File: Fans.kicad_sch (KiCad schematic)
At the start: 8 parts, among them J7 Conn_01x06, Q1 PSMN8R5-40MSDX, Q2 PSMN8R5-40MSDX

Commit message: schematic
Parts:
- removed Q1, Q2: PSMN8R5-40MSDX, BUK7M1780EX, symbol utsvt_power:PSMN8R5-40MSDX
- added D5, D7: 1N4148WT, Diode_SMD:D_SOD-523, symbol Diode:1N4148WT
- added D6, D9: LED, symbol Device:LED
- added LVPWR3, LVPWR4, LVPWR5, LVPWR6: LED, LED_SMD:LED_0603_1608Metric, symbol Device:LED
- added Q1, Q5: PSMN8R5-40MSDX, BUK7M1780EX, symbol Simulation_SPICE:NMOS
- added R15, R4, R5, R8: 260, symbol Device:R
- added R19, R20: 4.3k, symbol Device:R
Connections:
- net FANS_POS: now also D5.1 (K), D7.1 (K)
- net FAN_A_NEG: now also D6.1 (K), D7.2 (A), Q5.1 (D)
- net FAN_A_TACHO: now also R5.2
- net FAN_B_NEG: now also D5.2 (A), D9.1 (K), Q1.1 (D)
- net FAN_B_TACHO: now also R8.2
- net GND: now also LVPWR3.1 (K), LVPWR4.1 (K), LVPWR5.1 (K), LVPWR6.1 (K), Q1.3 (S), Q5.3 (S)
- net PWM_FAN_A: now also R4.2
- net PWM_FAN_B: now also R15.2
- net at R_G2.1, R_PD2.2: now also Q1.2 (G)
- net at R_G1.1, R_PD1.2: now also Q5.2 (G)
- new net: LVPWR5.2 (A), R8.1
- new net: D9.2 (A), R20.1
- new net: LVPWR6.2 (A), R15.1
- new net: LVPWR4.2 (A), R5.1
- new net: LVPWR3.2 (A), R4.1
- new net: D6.2 (A), R19.1
- new net +24V: R19.2, R20.2
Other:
- note added: "Flyback Diodes"
- note added: "Indicator LEDs"
- note added: "put close to fan connector and mosfet for small inductive loop"
- moved on the sheet: J7, R10, R_G1, R_PD1, R_PD2

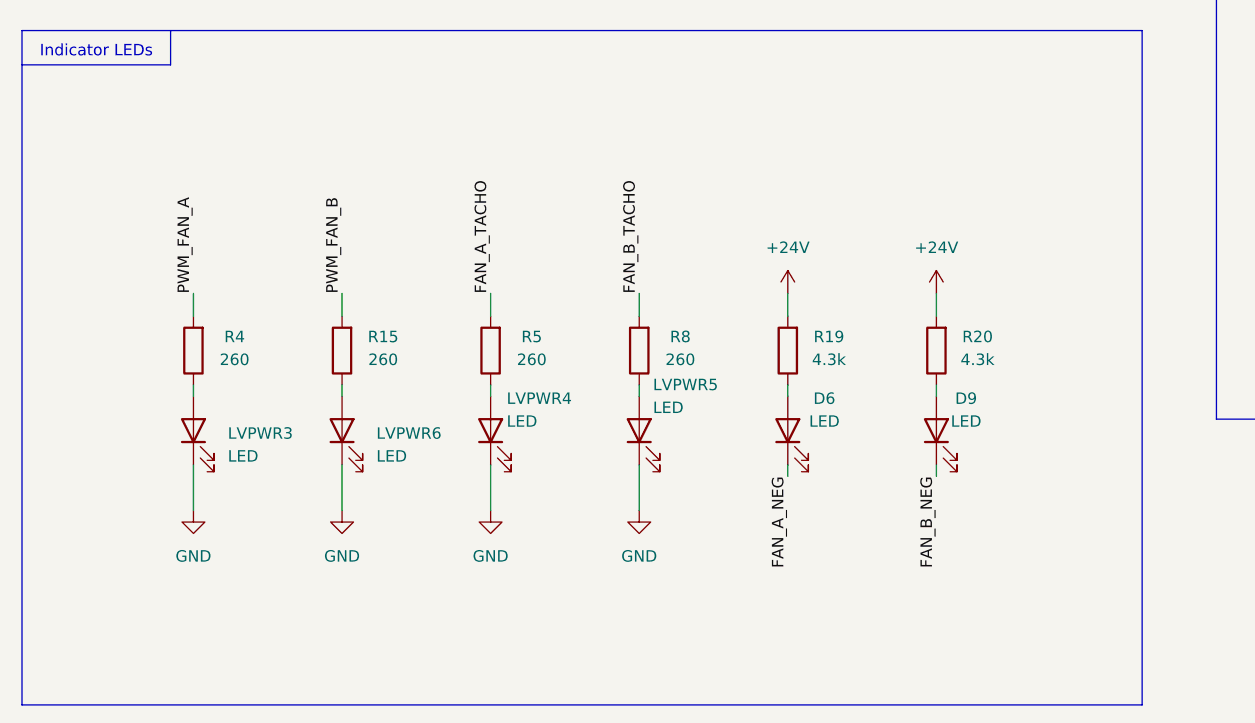
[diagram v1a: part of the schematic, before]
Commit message: added testpoints too
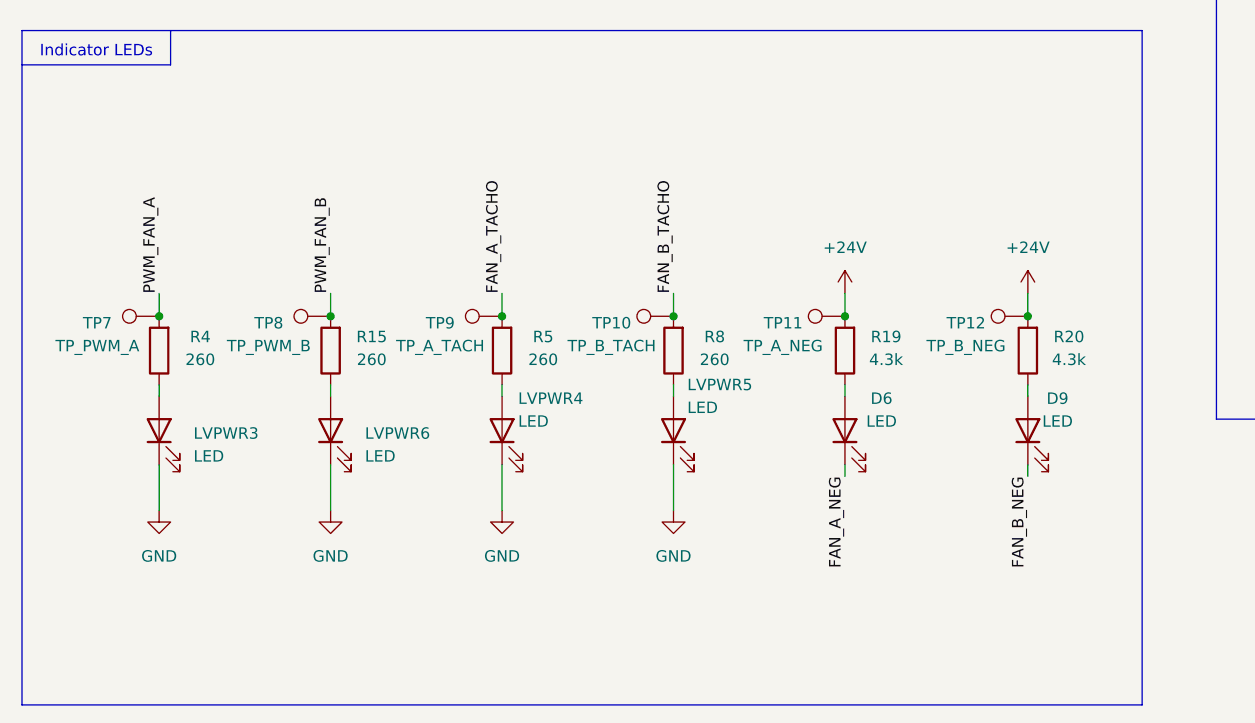
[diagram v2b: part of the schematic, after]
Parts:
- added TP10: TP_B_TACH, symbol Connector:TestPoint
- added TP11: TP_A_NEG, symbol Connector:TestPoint
- added TP12: TP_B_NEG, symbol Connector:TestPoint
- added TP7: TP_PWM_A, symbol Connector:TestPoint
- added TP8: TP_PWM_B, symbol Connector:TestPoint
- added TP9: TP_A_TACH, symbol Connector:TestPoint
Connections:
- net +24V: now also TP11.1, TP12.1
- net FAN_A_TACHO: now also TP9.1
- net FAN_B_TACHO: now also TP10.1
- net PWM_FAN_A: now also TP7.1
- net PWM_FAN_B: now also TP8.1
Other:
- moved on the sheet: D6, D9, LVPWR3, LVPWR4, LVPWR5, LVPWR6, R15, R19, R20, R4, R5, R8

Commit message: changes + ioc
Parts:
- removed LVPWR4, LVPWR5: LED, LED_SMD:LED_0603_1608Metric, symbol Device:LED
- removed R5, R8: 260, symbol Device:R
- removed TP10: TP_B_TACH, symbol Connector:TestPoint
- removed TP9: TP_A_TACH, symbol Connector:TestPoint
- R15, R4: value 260 -> 5k
- R19, R20: value 4.3k -> 5k
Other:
- moved on the sheet: D6, D9, LVPWR3, LVPWR6, R15, R19, R20, R4, TP11, TP12, TP7, TP8

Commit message: layout
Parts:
- removed D6, D9: LED, symbol Device:LED
- removed Q1, Q5: PSMN8R5-40MSDX, BUK7M1780EX, symbol Simulation_SPICE:NMOS
- added LVPWR16, LVPWR17: LED, LED_SMD:LED_0603_1608Metric, symbol Device:LED
- added Q1, Q5: PSMN8R5-40MSDX, UTSVT_Power:PSMN8R5-40MSDX, symbol UTSVT_Power:PSMN8R5-40MSDX
- D5, D7: Manufacturer_Part_Number (none) -> NCD0603R1
- J7: footprint (none) -> Connector_Molex:Molex_Nano-Fit_105310-xx06_2x03_P2.50mm_Vertical
- R10: footprint (none) -> Resistor_SMD:R_0603_1608Metric_Pad0.98x0.95mm_HandSolder; Manufacturer_Part_Number (none) -> CRCW06030000Z0EE
- R15, R19, R20, R4: value 5k -> 4.3k; footprint (none) -> Resistor_SMD:R_0603_1608Metric_Pad0.98x0.95mm_HandSolder; Manufacturer_Part_Number (none) -> CRCW06034K30FKEA
- R_G1, R_G2: footprint (none) -> Resistor_SMD:R_0603_1608Metric_Pad0.98x0.95mm_HandSolder; Manufacturer_Part_Number (none) -> CRCW0603120RFKEC
- R_PD1, R_PD2: footprint (none) -> Resistor_SMD:R_0603_1608Metric_Pad0.98x0.95mm_HandSolder; Manufacturer_Part_Number (none) -> CRCW060310K0FKEI
- TP11, TP12, TP7, TP8: footprint (none) -> TestPoint:TestPoint_Pad_1.0x1.0mm
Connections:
- net FAN_A_NEG: now also LVPWR16.1 (K), Q1.10 (D_6), Q1.11 (D_7), Q1.5 (D_1), Q1.6 (D_2), Q1.7 (D_3), Q1.8 (D_4), Q1.9 (D_5)
- net FAN_B_NEG: now also LVPWR17.1 (K), Q5.10 (D_6), Q5.11 (D_7), Q5.5 (D_1), Q5.6 (D_2), Q5.7 (D_3), Q5.8 (D_4), Q5.9 (D_5)
- net GND: now also Q1.1 (S_1), Q1.2 (S_2), Q1.3 (S_3), Q5.1 (S_1), Q5.2 (S_2), Q5.3 (S_3)
- net at R_G2.1, R_PD2.2: now also Q5.4 (G)
- net at R20.1: now also LVPWR17.2 (A)
- net at R_G1.1, R_PD1.2: now also Q1.4 (G)
- net at R19.1: now also LVPWR16.2 (A)
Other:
- moved on the sheet: R_G1, R_PD1

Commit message: added more
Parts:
- J7: footprint Connector_Molex:Molex_Nano-Fit_105310-xx06_2x03_P2.50mm_Vertical -> Connector_Molex:Molex_Nano-Fit_105309-xx06_1x06_P2.50mm_Vertical
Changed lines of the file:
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@@
 			)
 		)
-		(property "Footprint" "Connector_Molex:Molex_Nano-Fit_105310-xx06_2x03_P2.50mm_Vertical"
+		(property "Footprint" "Connector_Molex:Molex_Nano-Fit_105309-xx06_1x06_P2.50mm_Vertical"
 			(at 201.93 44.45 0)
 			(effects

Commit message: fon
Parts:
- renumbered TP7 to PWM_A2, TP8 to PWM_B2
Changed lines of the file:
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@@
 		(on_board yes)
 		(dnp no)
-		(property "Reference" "TP7"
+		(property "Reference" "PWM_A2"
 			(at 38.862 146.812 90)
 			(effects
@@
 			(project ""
 				(path "/a2e13c19-ff3a-4e43-a7f5-200fd5b2b978/26b9ca43-4422-48e7-9562-1bb32842f27e"
-					(reference "TP7")
+					(reference "PWM_A2")
 					(unit 1)
 				)
@@
 		(on_board yes)
 		(dnp no)
-		(property "Reference" "TP8"
+		(property "Reference" "PWM_B2"
 			(at 57.912 146.812 90)
 			(effects
@@
 			(project "PS-MotorControllerInterfacePCB"
 				(path "/a2e13c19-ff3a-4e43-a7f5-200fd5b2b978/26b9ca43-4422-48e7-9562-1bb32842f27e"
-					(reference "TP8")
-					(unit 1)
-				)
+					(reference "PWM_B2")
+					(unit 1)
+				)

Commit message: hello
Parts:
- removed TP11: TP_A_NEG, TestPoint:TestPoint_Pad_1.0x1.0mm, symbol Connector:TestPoint
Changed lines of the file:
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@@
 	)
 	(junction
-		(at 86.36 146.05)
-		(diameter 0)
-		(color 0 0 0 0)
-	)
-	(junction
 		(at 64.77 146.05)
 		(diameter 0)
@@
 					(unit 1)
 				)
-			)
-		)
-	)
-	(symbol
-		(lib_id "Connector:TestPoint")
-		(at 86.36 146.05 90)
-		(unit 1)
-		(exclude_from_sim no)
-		(in_bom yes)
-		(on_board yes)
-		(dnp no)
-		(property "Reference" "TP11"
-			(at 79.502 146.812 90)
-			(effects
-				(font
-					(size 1.27 1.27)
-				)
-			)
-		)
-		(property "Value" "TP_A_NEG"
-			(at 79.502 149.352 90)
-			(effects
-				(font
-					(size 1.27 1.27)
-				)
-			)
-		)
-		(property "Footprint" "TestPoint:TestPoint_Pad_1.0x1.0mm"
-			(at 86.36 140.97 0)
-			(effects
-				(font
-					(size 1.27 1.27)
-				)
-				(hide yes)
-			)
-		)
-		(property "Datasheet" "~"
-			(at 86.36 140.97 0)
-			(effects
-				(font
-					(size 1.27 1.27)
-				)
-				(hide yes)
-			)
-		)
-		(property "Description" "test point"
-			(at 86.36 146.05 0)
-			(effects
-				(font
-					(size 1.27 1.27)
-				)
-				(hide yes)
-			)
-		)
-		(property "Manufacturer" ""
-			(at 86.36 146.05 90)
-			(effects
-				(font
-					(size 1.27 1.27)
-				)
-				(hide yes)
-			)
-		)
-		(property "Mouser Link" ""
-			(at 86.36 146.05 90)
-			(effects
-				(font
-					(size 1.27 1.27)
-				)
-				(hide yes)
-			)
-		)
-		(pin "1"
-		)
-		(instances
-			(project "PS-MotorControllerInterfacePCB"
-				(path "/a2e13c19-ff3a-4e43-a7f5-200fd5b2b978/26b9ca43-4422-48e7-9562-1bb32842f27e"
-					(reference "TP11")
-					(unit 1)
-				)

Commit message: done
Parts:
- J7: Mouser Part Number (none) -> 538-105309-1206
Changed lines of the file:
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@@
+			)
+		)
+		(property "Sim.Type" ""
+			(at 96.52 66.04 90)
+			(effects
+				(font
+					(size 1.27 1.27)
+				)
+				(hide yes)
 			)
 		)
@@
 			)
 		)
+		(property "Sim.Type" ""
+			(at 44.45 50.8 0)
+			(effects
+				(font
+					(size 1.27 1.27)
+				)
+				(hide yes)
+			)
+		)
 		(pin "8"
 		)
@@
 			)
 		)
+		(property "Sim.Type" ""
+			(at 86.36 158.75 90)
+			(effects
+				(font
+					(size 1.27 1.27)
+				)
+				(hide yes)
+			)
+		)
 		(pin "1"
 		)
@@
 			)
 		)
+		(property "Sim.Type" ""
+			(at 106.68 149.86 0)
+			(effects
+				(font
+					(size 1.27 1.27)
+				)
+				(hide yes)
+			)
+		)
 		(pin "1"
 		)
@@
 			)
 		)
+		(property "Sim.Type" ""
+			(at 64.77 158.75 90)
+			(effects
+				(font
+					(size 1.27 1.27)
+				)
+				(hide yes)
+			)
+		)
 		(pin "1"
 		)
@@
 			)
 		)
+		(property "Sim.Type" ""
+			(at 34.29 62.23 90)
+			(effects
+				(font
+					(size 1.27 1.27)
+				)
+				(hide yes)
+			)
+		)
 		(pin "2"
 		)
@@
 			)
 		)
+		(property "Sim.Type" ""
+			(at 64.77 149.86 0)
+			(effects
+				(font
+					(size 1.27 1.27)
+				)
+				(hide yes)
+			)
+		)
 		(pin "1"
 		)
@@
 			)
 		)
+		(property "Sim.Type" ""
+			(at 88.9 62.23 90)
+			(effects
+				(font
+					(size 1.27 1.27)
+				)
+				(hide yes)
+			)
+		)
 		(pin "2"
 		)
@@
 		)
 		(property "Mouser Link" ""
+			(at 106.68 146.05 90)
+			(effects
+				(font
+					(size 1.27 1.27)
+				)
+				(hide yes)
+			)
+		)
+		(property "Sim.Type" ""
 			(at 106.68 146.05 90)
 			(effects
@@
 			)
 		)
+		(property "Sim.Type" ""
+			(at 196.85 111.76 90)
+			(effects
+				(font
+					(size 1.27 1.27)
+				)
+				(hide yes)
+			)
+		)
 		(pin "2"
 		)
@@
 			)
 		)
+		(property "Sim.Type" ""
+			(at 45.72 158.75 90)
+			(effects
+				(font
+					(size 1.27 1.27)
+				)
+				(hide yes)
+			)
+		)
 		(pin "1"
 		)
@@
 			)
 		)
+		(property "Sim.Type" ""
+			(at 45.72 146.05 90)
+			(effects
+				(font
+					(size 1.27 1.27)
+				)
+				(hide yes)
+			)
+		)
 		(pin "1"
 		)
@@
 			)
 		)
+		(property "Sim.Type" ""
+			(at 45.72 149.86 0)
+			(effects
+				(font
+					(size 1.27 1.27)
+				)
+				(hide yes)
+			)
+		)
 		(pin "1"
 		)
@@
 		)
 		(property "Manufacturer_Part_Number" "CRCW06034K30FKEA"
+			(at 86.36 149.86 0)
+			(effects
+				(font
+					(size 1.27 1.27)
+				)
+				(hide yes)
+			)
+		)
+		(property "Sim.Type" ""
 			(at 86.36 149.86 0)
 			(effects
@@
 			)
 		)
+		(property "Sim.Type" ""
+			(at 106.68 158.75 90)
+			(effects
+				(font
+					(size 1.27 1.27)
+				)
+				(hide yes)
+			)
+		)
 		(pin "1"
 		)
@@
 			)
 		)
+		(property "Sim.Type" ""
+			(at 41.91 66.04 90)
+			(effects
+				(font
+					(size 1.27 1.27)
+				)
+				(hide yes)
+			)
+		)
 		(pin "2"
 		)
@@
 			)
 		)
-		(property "Datasheet" "~"
+		(property "Datasheet" ""
 			(at 201.93 44.45 0)
 			(effects
@@
 		)
 		(property "Mouser Link" ""
+			(at 201.93 44.45 0)
+			(effects
+				(font
+					(size 1.27 1.27)
+				)
+				(hide yes)
+			)
+		)
+		(property "Sim.Type" ""
+			(at 201.93 44.45 0)
+			(effects
+				(font
+					(size 1.27 1.27)
+				)
+				(hide yes)
+			)
+		)
+		(property "Mouser Part Number" "538-105309-1206"
 			(at 201.93 44.45 0)
 			(effects
@@
 			)
 		)
+		(property "Sim.Type" ""
+			(at 196.85 128.27 90)
+			(effects
+				(font
+					(size 1.27 1.27)
+				)
+				(hide yes)
+			)
+		)
 		(pin "2"
 		)
@@
 		)
 		(property "Mouser Link" ""
+			(at 64.77 146.05 90)
+			(effects
+				(font
+					(size 1.27 1.27)
+				)
+				(hide yes)
+			)
+		)
+		(property "Sim.Type" ""
 			(at 64.77 146.05 90)
 			(effects
@@
 			)
 		)
+		(property "Sim.Type" ""
+			(at 76.2 85.09 90)
+			(effects
+				(font
+					(size 1.27 1.27)
+				)
+				(hide yes)
+			)
+		)
 		(pin "1"
 		)
@@
 			(at 99.06 50.8 0)
 			(effects
+				(font
+					(size 1.27 1.27)
+				)
+				(hide yes)
+			)
+		)
+		(property "Sim.Type" ""
+			(at 99.06 50.8 0)
+			(effects
